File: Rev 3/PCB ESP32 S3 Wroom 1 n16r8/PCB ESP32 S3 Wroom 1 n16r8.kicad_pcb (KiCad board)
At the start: 2 copper layers, 80.5 x 89.5 mm, 36 parts, among them IC1 LM2675N-3.3_NOPB, J1 AudioJack3_SwitchT, M1 Haptic Feedback, Q1 BS170, SW1 Home, SW2 Back, SW3 Play/Pause, SW4 Power, SW5 Menu, SW6 Hold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

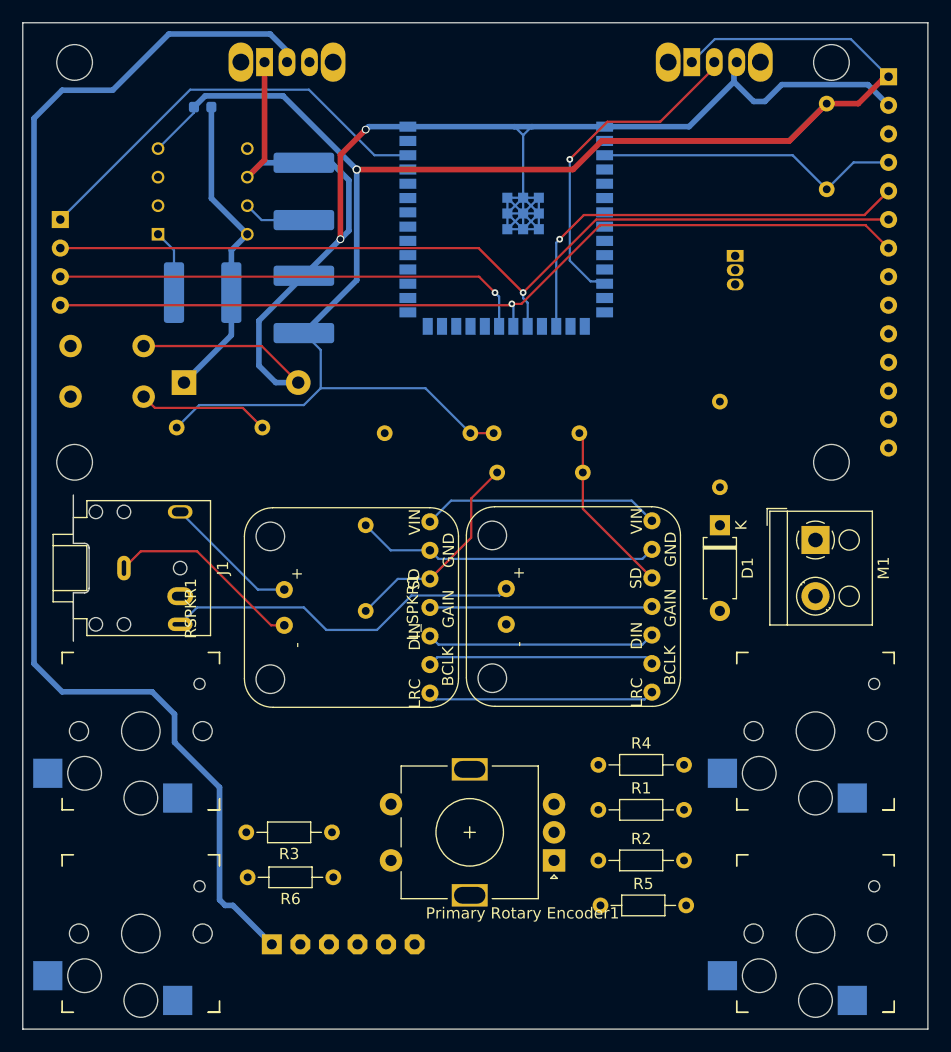
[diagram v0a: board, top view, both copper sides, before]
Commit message: Routed more vias
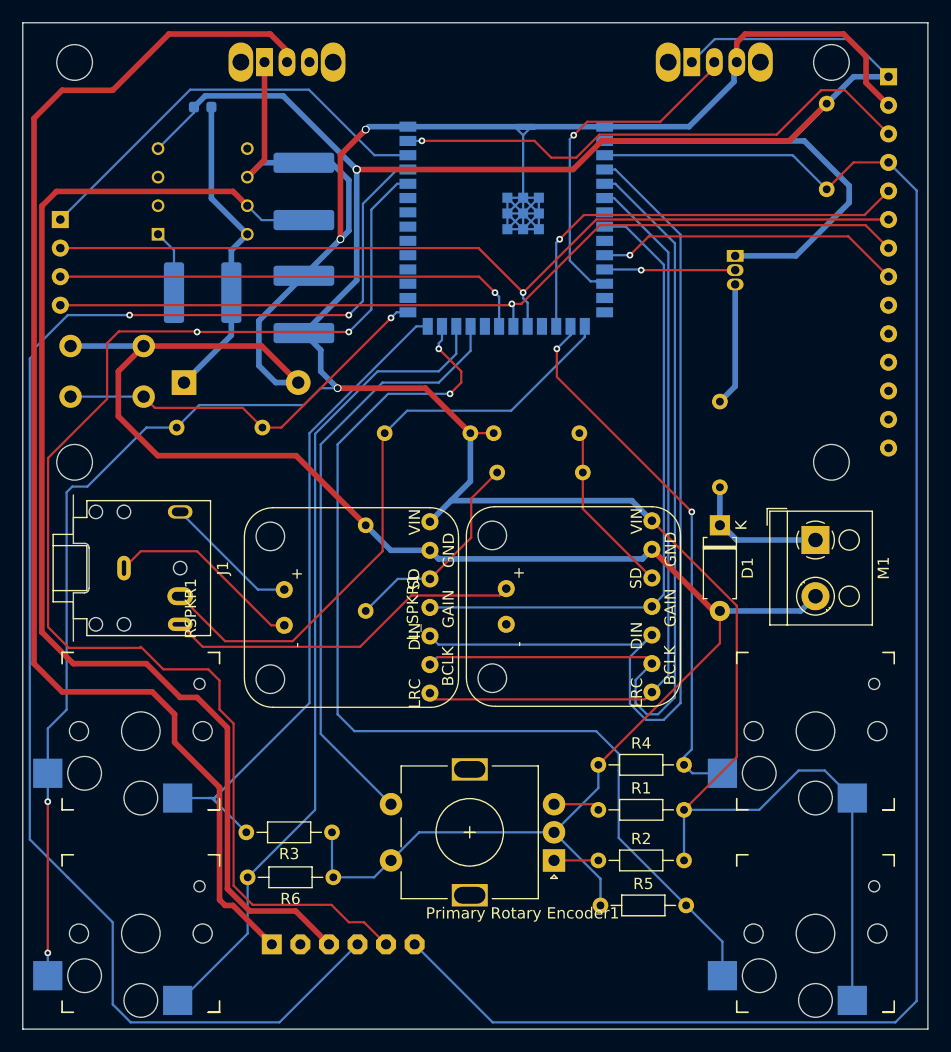
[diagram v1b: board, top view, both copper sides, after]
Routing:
- net /VDD: track 188.8 -> 343.5 mm, vias 1 -> 4
- net /TXD: track 0.00 -> 132.0 mm, vias 0 -> 2
- net /RESET: track 27.5 -> 151.4 mm
- net GND: track 190.4 -> 312.2 mm
- net /RXD: track 0.00 -> 117.1 mm, vias 0 -> 2
- net /5V: track 5.56 -> 108.2 mm
- net /MENU_BUTTON: track 0.00 -> 93.2 mm, vias 0 -> 2
- net /BACK_BUTTON: track 0.00 -> 73.6 mm
- net /DAC_DIN: track 20.4 -> 83.8 mm
- net /HOME_BUTTON: track 0.00 -> 59.2 mm
- net /DAC_BCLK: track 20.3 -> 77.7 mm
- net /Detect_Jack: track 0.00 -> 55.8 mm
- net Net-(X1-IO21): track 0.00 -> 53.5 mm
- net /PLAY/PAUSE BUTTON: track 0.00 -> 48.5 mm, vias 0 -> 2
- net /TFT_CS: track 0.00 -> 47.5 mm, vias 0 -> 1
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
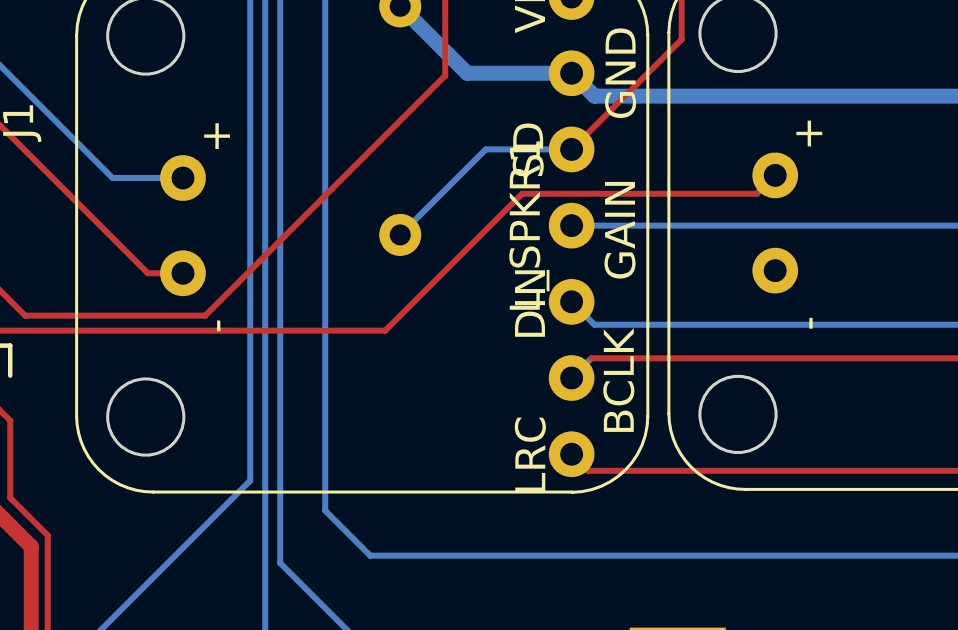
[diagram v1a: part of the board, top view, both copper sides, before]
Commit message: routed more vias
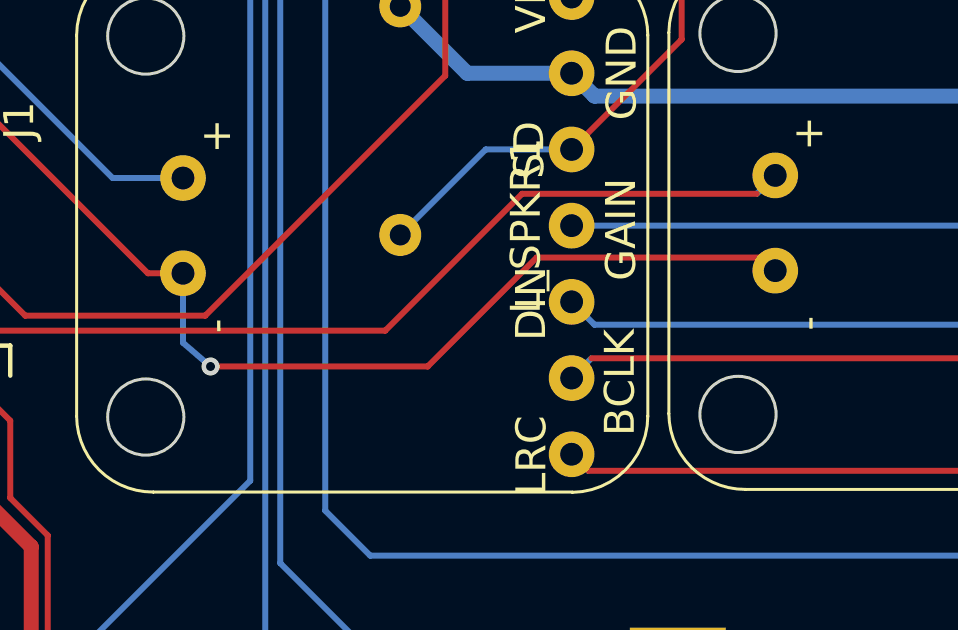
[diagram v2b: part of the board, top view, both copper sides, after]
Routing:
- net Net-(L_SPKR1-SPKR-): track 18.3 -> 42.4 mm, vias 0 -> 1
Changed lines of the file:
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@@
+	)
+	(segment
+		(start 93.549 96.062)
+		(end 101.062 96.062)
+		(width 0.2)
+		(layer "F.Cu")
+		(net 16)
 	)
 	(segment
@@
 	)
 	(segment
+		(start 89.916 99.695)
+		(end 93.549 96.062)
+		(width 0.2)
+		(layer "F.Cu")
+		(net 16)
+	)
+	(segment
+		(start 82.677 99.695)
+		(end 89.916 99.695)
+		(width 0.2)
+		(layer "F.Cu")
+		(net 16)
+	)
+	(segment
+		(start 101.062 96.062)
+		(end 101.5 96.5)
+		(width 0.2)
+		(layer "F.Cu")
+		(net 16)
+	)
+	(segment
 		(start 81.7585 96.5875)
 		(end 80.5875 96.5875)
 		(width 0.2)
 		(layer "F.Cu")
+		(net 16)
+	)
+	(via
+		(at 82.677 99.695)
+		(size 0.6)
+		(drill 0.3)
+		(layers "F.Cu" "B.Cu")
 		(net 16)
 	)
@@
 	)
 	(segment
+		(start 81.7585 98.9035)
+		(end 82.677 99.695)
+		(width 0.2)
+		(layer "B.Cu")
+		(net 16)
+	)
+	(segment
 		(start 82.036 96.31)
 		(end 81.7585 96.5875)
 		(width 0.2)
 		(layer "B.Cu")
+		(net 16)
+	)
+	(segment
+		(start 81.7585 96.5875)
+		(end 81.7585 98.9035)
+		(width 0.2)
+		(layer "B.Cu")
+		(net 16)
+	)
+	(segment
+		(start 82.677 99.695)
+		(end 82.55 99.695)
+		(width 0.2)
+		(layer "B.Cu")

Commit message: finished traces
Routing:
- net Net-(X1-IO7): track 3.94 -> 85.4 mm, vias 0 -> 1
- net Net-(X1-IO16): track 4.15 -> 84.6 mm, vias 0 -> 1
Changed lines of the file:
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@@
+	)
+	(segment
+		(start 112.13 61.13)
+		(end 114.427 63.427)
+		(width 0.2)
+		(layer "B.Cu")
+		(net 19)
+	)
+	(segment
+		(start 114.427 67.945)
+		(end 115.516 69.034)
+		(width 0.2)
+		(layer "B.Cu")
+		(net 19)
+	)
+	(segment
+		(start 115.516 69.034)
+		(end 115.516 93.8505)
+		(width 0.2)
+		(layer "B.Cu")
+		(net 19)
+	)
+	(segment
+		(start 114.427 63.427)
+		(end 114.427 67.945)
+		(width 0.2)
+		(layer "B.Cu")
+		(net 19)
 	)
 	(segment
 		(start 115.516 93.8505)
-		(end 115.516 64.516)
-		(width 0.2)
-		(layer "B.Cu")
-		(net 19)
-	)
-	(segment
-		(start 112.13 61.13)
-		(end 110.25 61.13)
+		(end 114.454 94.9125)
 		(width 0.2)
 		(layer "B.Cu")
@@
 	)
 	(segment
-		(start 114.454 94.9125)
-		(end 115.516 93.8505)
-		(width 0.2)
-		(layer "B.Cu")
-		(net 19)
-	)
-	(segment
 		(start 114.3665 95)
 		(end 114.454 94.9125)
@@
 	)
 	(segment
-		(start 115.516 64.516)
+		(start 110.25 61.13)
 		(end 112.13 61.13)
 		(width 0.2)
@@
 	)
 	(segment
+		(start 122.428 69.85)
+		(end 126.746 74.168)
+		(width 0.2)
+		(layer "F.Cu")
+		(net 24)
+	)
+	(segment
+		(start 126.746 74.168)
+		(end 126.746 111.379)
+		(width 0.2)
+		(layer "F.Cu")
+		(net 24)
+	)
+	(segment
+		(start 126.746 111.379)
+		(end 122.301 115.824)
+		(width 0.2)
+		(layer "F.Cu")
+		(net 24)
+	)
+	(segment
+		(start 117.983 69.85)
+		(end 122.428 69.85)
+		(width 0.2)
+		(layer "F.Cu")
+		(net 24)
+	)
+	(segment
+		(start 115.189 67.056)
+		(end 117.983 69.85)
+		(width 0.2)
+		(layer "F.Cu")
+		(net 24)
+	)
+	(segment
 		(start 105.75 117.5)
 		(end 109.69 117.5)
@@
 	)
 	(segment
+		(start 111.366 115.824)
+		(end 109.69 117.5)
+		(width 0.2)
+		(layer "F.Cu")
+		(net 24)
+	)
+	(segment
+		(start 122.301 115.824)
+		(end 111.366 115.824)
+		(width 0.2)
+		(layer "F.Cu")
+		(net 24)
+	)
+	(via
+		(at 115.189 67.056)
+		(size 0.6)
+		(drill 0.3)
+		(layers "F.Cu" "B.Cu")
+		(net 24)
+	)
+	(segment
+		(start 115.189 63.623314)
+		(end 115.189 67.056)
+		(width 0.2)
+		(layer "B.Cu")
+		(net 24)
+	)
+	(segment
+		(start 110.25 59.86)
+		(end 111.425686 59.86)
+		(width 0.2)
+		(layer "B.Cu")
+		(net 24)
+	)
+	(segment
+		(start 110.166 59.944)
+		(end 110.109 59.944)
+		(width 0.2)
+		(layer "B.Cu")
+		(net 24)
+	)
+	(segment
+		(start 111.425686 59.86)
+		(end 115.189 63.623314)
+		(width 0.2)
+		(layer "B.Cu")
+		(net 24)
+	)
+	(segment
+		(start 110.25 59.86)
+		(end 110.166 59.944)
+		(width 0.2)
+		(layer "B.Cu")
+		(net 24)
+	)
+	(segment
 		(start 98.325 72.175)
 		(end 98.325 70)
@@
 	)
 	(segment
+		(start 122.301 114.681)
+		(end 126.111 110.871)
+		(width 0.2)
+		(layer "F.Cu")
+		(net 26)
+	)
+	(segment
+		(start 126.111 74.549)
+		(end 122.047 70.485)
+		(width 0.2)
+		(layer "F.Cu")
+		(net 26)
+	)
+	(segment
+		(start 111.371 114.681)
+		(end 122.301 114.681)
+		(width 0.2)
+		(layer "F.Cu")
+		(net 26)
+	)
+	(segment
+		(start 114.808 70.485)
+		(end 108.204 63.881)
+		(width 0.2)
+		(layer "F.Cu")
+		(net 26)
+	)
+	(segment
+		(start 126.111 110.871)
+		(end 126.111 74.549)
+		(width 0.2)
+		(layer "F.Cu")
+		(net 26)
+	)
+	(segment
+		(start 122.047 70.485)
+		(end 114.808 70.485)
+		(width 0.2)
+		(layer "F.Cu")
+		(net 26)
+	)
+	(segment
 		(start 109.19 112.5)
 		(end 109.69 113)
@@
 		(net 26)
 	)
+	(segment
+		(start 108.204 63.881)
+		(end 108.077 63.754)
+		(width 0.2)
+		(layer "F.Cu")
+		(net 26)
+	)
+	(segment
+		(start 109.69 113)
+		(end 111.371 114.681)
+		(width 0.2)
+		(layer "F.Cu")
+		(net 26)
+	)
+	(via
+		(at 108.204 63.881)
+		(size 0.6)
+		(drill 0.3)
+		(layers "F.Cu" "B.Cu")
+		(net 26)
+	)
+	(segment
+		(start 108.204 63.496)
+		(end 108.204 63.881)
+		(width 0.2)
+		(layer "B.Cu")
+		(net 26)
+	)
+	(segment
+		(start 110.25 62.4)
+		(end 109.3 62.4)
+		(width 0.2)
+		(layer "B.Cu")
+		(net 26)
+	)
+	(segment
+		(start 109.3 62.4)
+		(end 108.204 63.496)
+		(width 0.2)
+		(layer "B.Cu")
+		(net 26)
+	)

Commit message: updated d2 footprint
-1A, 40 V Schottky rectifier per datasheet
-package size determined from digikey
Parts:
- D2: value SB120 -> 1A, 40 V Schottky rectifier; footprint Diode_THT:D_DO-41_SOD81_P10.16mm_Horizontal -> Diode_SMD:D_SOD-323_HandSoldering
- moved D2 5.81 mm to (78.3, 72.9)
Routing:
- net GND: track 312.2 -> 302.2 mm, vias 2 -> 3
- net Net-(D2-K): track 28.2 -> 24.3 mm

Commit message: updated inductor footprint
to be a standard 2424 (6060 metric) mount for a power rectifier.
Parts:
- L1: footprint Capacitor_SMD:C_0603_1608Metric -> Inductor_SMD:L_Coilcraft_XAL6060-XXX
- moved L1 10.4 mm to (65.5, 55.8), turned to -90 degrees
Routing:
- net /VDD: track 343.5 -> 349.8 mm
- net /SD_CS: track 38.1 -> 44.2 mm
- net Net-(D2-K): track 24.3 -> 25.5 mm

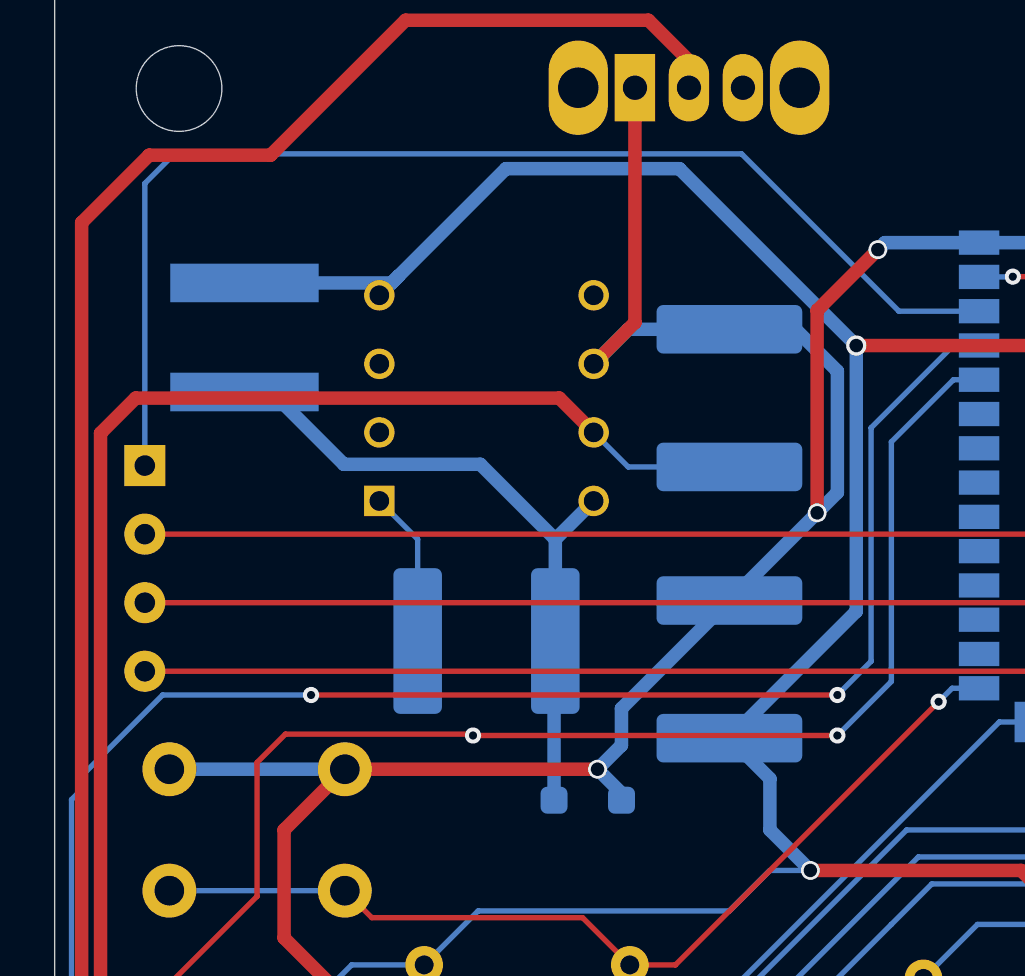
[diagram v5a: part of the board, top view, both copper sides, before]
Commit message: changed out power regulator
- JLCPCB part package sizes
- new chip supports 4.5v-36v so it will work with usb power
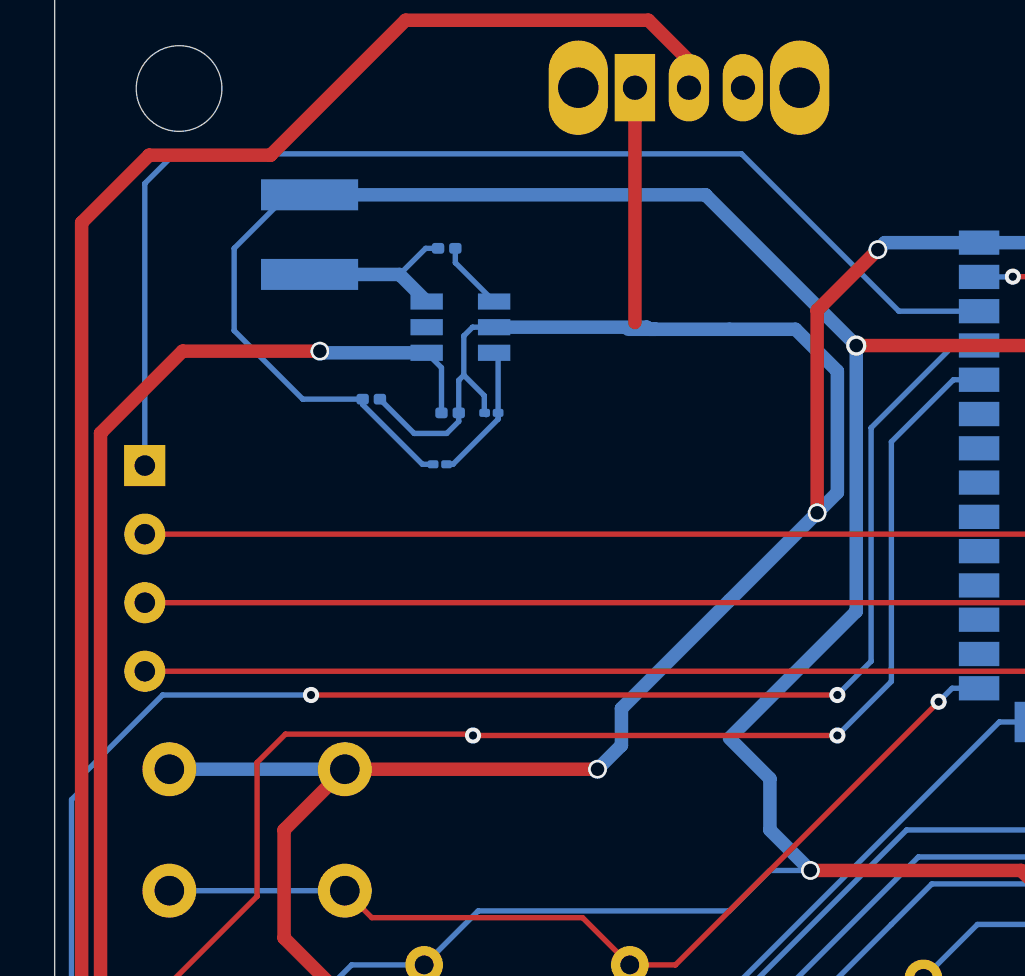
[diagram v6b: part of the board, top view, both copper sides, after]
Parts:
- removed D2: 1A, 40 V Schottky rectifier, Diode_SMD:D_SOD-323_HandSoldering
- removed IC1: LM2675N-3.3_NOPB, LM2675-3.3:DIP794W53P254L959H508Q8N
- added R14: 69.8K, Resistor_SMD:R_01005_0402Metric, B.Cu at (72.8, 60.5)
- added R15: 22.1K, Resistor_SMD:R_01005_0402Metric, B.Cu at (74.7, 58.5)
- added U1: LMR54410DBVR, LMR54410DBVR:SOT95P280X145-6N, B.Cu at (73.5, 55.4)
- C1: value 10 nF -> .1 uF; footprint Capacitor_SMD:C_2220_5750Metric -> Capacitor_SMD:C_0201_0603Metric
- C2: value 100 uF -> 2.2 uF; footprint Capacitor_SMD:C_2220_5750Metric -> Capacitor_SMD:C_0201_0603Metric
- C3: value 68uF -> 10uF; footprint Capacitor_SMD:C_2220_5750Metric -> Capacitor_SMD:C_0201_0603Metric
- L1: value 47uH -> 15uH; footprint Inductor_SMD:L_Coilcraft_XAL6060-XXX -> Inductor_SMD:L_Vishay_IFSC-1515AH_4x4x1.8mm
- moved C3 16.6 mm to (70.2, 58.0), turned to 180 degrees
- moved C1 14.6 mm to (73.0, 52.5), turned to 0 degrees
- moved C2 10.4 mm to (73.2, 58.5), turned to 180 degrees
- moved L1 4.51 mm to (67.9, 51.9)
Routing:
- net Net-(U1-SW): track 25.5 -> 6.58 mm
- net GND: track 302.2 -> 312.9 mm
- net /VDD: track 349.8 -> 359.7 mm
- net /5V: track 108.2 -> 99.2 mm, vias 0 -> 1
- net Net-(U1-FB): track 0.00 -> 5.12 mm
- net Net-(U1-CB): track 5.78 -> 2.57 mm
